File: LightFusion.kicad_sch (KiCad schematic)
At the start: 41 parts, among them IC2 ADS1292IPBSR, U1 BMD-350-A-R

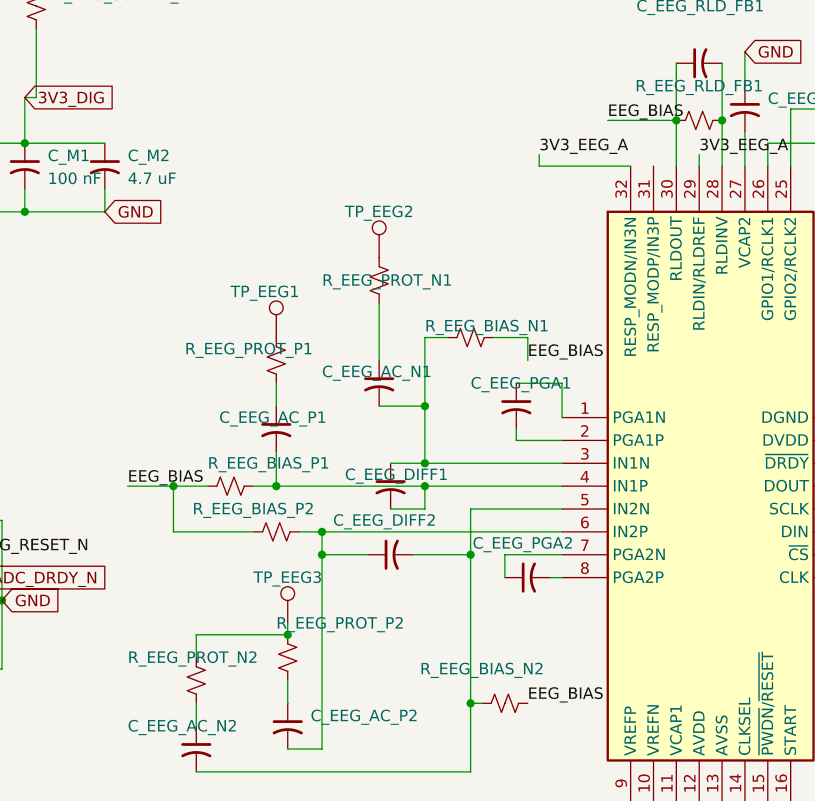
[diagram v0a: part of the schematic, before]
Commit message: remove silk screen removed from pcb
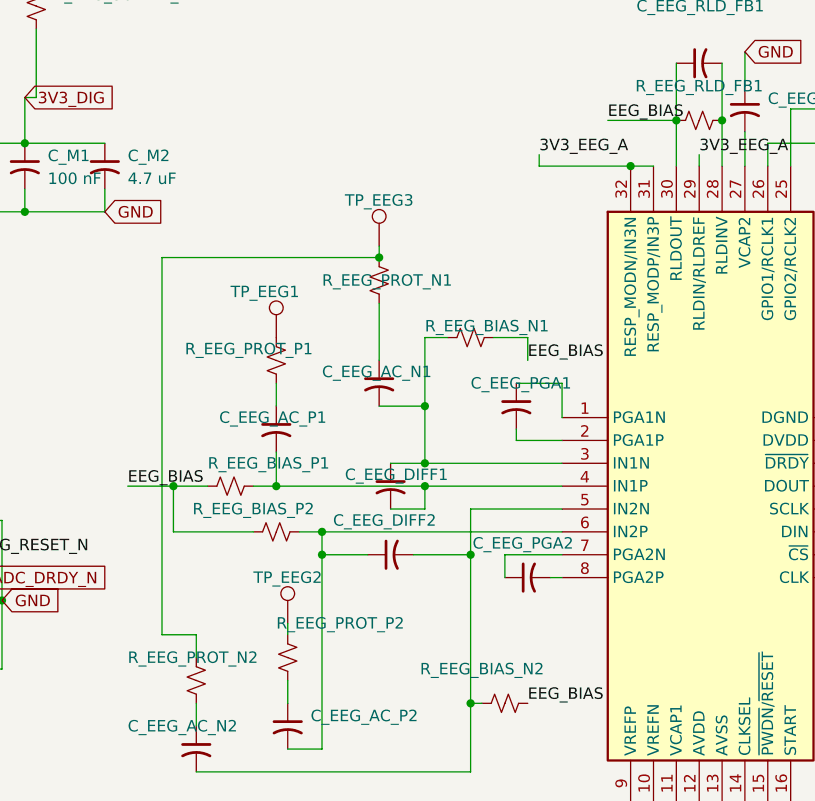
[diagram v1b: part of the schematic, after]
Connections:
- net 3V3_EEG_A: now also IC2.31 (RESP_MODP/IN3P)
- net at R_EEG_PROT_N1.1: now also R_EEG_PROT_N2.1, TP_EEG3.1; no longer TP_EEG2.1
- new net: R_EEG_PROT_P2.1, TP_EEG2.1
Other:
- moved on the sheet: TP_EEG2, TP_EEG3
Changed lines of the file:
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@@
 	)
 	(junction
+		(at 205.74 63.5)
+		(diameter 0)
+		(color 0 0 0 0)
+	)
+	(junction
 		(at 187.96 123.19)
 		(diameter 0)
@@
 	)
 	(junction
-		(at 167.64 115.57)
-		(diameter 0)
-		(color 0 0 0 0)
-	)
-	(junction
 		(at 210.82 58.42)
 		(diameter 0)
@@
 	)
 	(junction
+		(at 177.8 73.66)
+		(diameter 0)
+		(color 0 0 0 0)
+	)
+	(junction
 		(at 229.87 152.4)
 		(diameter 0)
@@
 	(wire
 		(pts
+			(xy 153.67 73.66) (xy 177.8 73.66)
+		)
+		(stroke
+			(width 0)
+			(type default)
+		)
+	)
+	(wire
+		(pts
 			(xy 171.45 106.68) (xy 176.53 106.68)
 		)
@@
 	(wire
 		(pts
+			(xy 205.74 63.5) (xy 208.28 63.5)
+		)
+		(stroke
+			(width 0)
+			(type default)
+		)
+	)
+	(wire
+		(pts
 			(xy 154.94 99.06) (xy 158.75 99.06)
 		)
@@
 	(wire
 		(pts
-			(xy 167.64 115.57) (xy 157.48 115.57)
-		)
-		(stroke
-			(width 0)
-			(type default)
-		)
-	)
-	(wire
-		(pts
 			(xy 208.28 137.16) (xy 205.74 137.16)
 		)
@@
 	(wire
 		(pts
+			(xy 153.67 115.57) (xy 153.67 73.66)
+		)
+		(stroke
+			(width 0)
+			(type default)
+		)
+	)
+	(wire
+		(pts
 			(xy 223.52 57.15) (xy 257.81 57.15)
 		)
@@
 	(wire
 		(pts
+			(xy 177.8 72.39) (xy 177.8 73.66)
+		)
+		(stroke
+			(width 0)
+			(type default)
+		)
+	)
+	(wire
+		(pts
 			(xy 251.46 144.78) (xy 251.46 147.32)
 		)
@@
 	(wire
 		(pts
+			(xy 157.48 115.57) (xy 153.67 115.57)
+		)
+		(stroke
+			(width 0)
+			(type default)
+		)
+	)
+	(wire
+		(pts
 			(xy 168.91 104.14) (xy 171.45 104.14)
 		)
@@
 	(symbol
 		(lib_id "TestPoint:TestPoint")
-		(at 177.8 73.66 0)
+		(at 167.64 114.3 0)
 		(unit 1)
 		(body_style 1)
@@
 		(dnp no)
 		(property "Reference" "TP_EEG2"
-			(at 173.99 68.58 0)
+			(at 163.83 109.22 0)
 			(show_name no)
 			(do_not_autoplace no)
@@
 		)
 		(property "Value" "TestPoint"
-			(at 180.34 71.6279 0)
+			(at 170.18 112.2679 0)
 			(hide yes)
 			(show_name no)
@@
 		)
 		(property "Footprint" "LightFusion:MILL-MAX_0906-0-15-20-76-14-11-0"
-			(at 182.88 73.66 0)
+			(at 172.72 114.3 0)
 			(hide yes)
 			(show_name no)
@@
 		)
 		(property "Datasheet" ""
-			(at 182.88 73.66 0)
+			(at 172.72 114.3 0)
 			(hide yes)
 			(show_name no)
@@
 		)
 		(property "Description" "test point"
-			(at 177.8 73.66 0)
+			(at 167.64 114.3 0)
 			(hide yes)
 			(show_name no)
@@
 	(symbol
 		(lib_id "TestPoint:TestPoint")
-		(at 167.64 114.3 0)
+		(at 177.8 72.39 0)
 		(unit 1)
 		(body_style 1)
@@
 		(dnp no)
 		(property "Reference" "TP_EEG3"
-			(at 163.83 109.22 0)
+			(at 173.99 67.31 0)
 			(show_name no)
 			(do_not_autoplace no)
@@
 		)
 		(property "Value" "TestPoint"
-			(at 170.18 112.2679 0)
+			(at 180.34 70.3579 0)
 			(hide yes)
 			(show_name no)
@@
 		)
 		(property "Footprint" "LightFusion:MILL-MAX_0906-0-15-20-76-14-11-0"
-			(at 172.72 114.3 0)
+			(at 182.88 72.39 0)
 			(hide yes)
 			(show_name no)
@@
 		)
 		(property "Datasheet" ""
-			(at 172.72 114.3 0)
+			(at 182.88 72.39 0)
 			(hide yes)
 			(show_name no)
@@
 		)
 		(property "Description" "test point"
-			(at 167.64 114.3 0)
+			(at 177.8 72.39 0)
 			(hide yes)
 			(show_name no)

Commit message: final verifications
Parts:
- added C_STIM_VCC1, C_STIM_VM1: 100 nF, LightFusion:C_0603_1608Metric, symbol C_Small_US:C_Small_US
- added C_STIM_VM2: 1 µF, LightFusion:C_0603_1608Metric, symbol C_Small_US:C_Small_US
- added R_SLEEP_PD1, R_STIM_IN1, R_STIM_IN2: 100 kΩ, LightFusion:R_0603_1608Metric, symbol R_Small_US:R_Small_US
- added R_STIM_N1, R_STIM_P1: 22 kΩ, LightFusion:R_0603_1608Metric, symbol R_Small_US:R_Small_US
- added R_STIM_PD1, R_STIM_PD2: 1 MΩ, LightFusion:R_0603_1608Metric, symbol R_Small_US:R_Small_US
- added STIM_E_N1, STIM_E_P1: (no value), LightFusion:MILL-MAX_0906-0-15-20-76-14-11-0, symbol Electrode_MillMax_0906:Electrode_MillMax_0906
- added U4: DRV8837DSGR, LightFusion:DRV8837DSGR, symbol DRV8837DSGR:DRV8837DSGR
- E_EEG1: renamed from TP_EEG1; value TestPoint -> (none); symbol TestPoint:TestPoint -> Electrode_MillMax_0906:Electrode_MillMax_0906; now not fitted
- E_EEG2: renamed from TP_EEG2; value TestPoint -> (none); symbol TestPoint:TestPoint -> Electrode_MillMax_0906:Electrode_MillMax_0906; now not fitted
- E_EEG3: renamed from TP_EEG3; value TestPoint -> (none); symbol TestPoint:TestPoint -> Electrode_MillMax_0906:Electrode_MillMax_0906; now not fitted
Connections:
- net 3V3_DIG: now also C_STIM_VCC1.1, U4.8 (VCC)
- net GND: now also C_STIM_VCC1.2, C_STIM_VM1.2, C_STIM_VM2.2, R_SLEEP_PD1.1, R_STIM_IN1.2, R_STIM_IN2.2, R_STIM_PD1.2, R_STIM_PD2.2, U4.4 (GND), U4.9 (EXP)
- net MCU_STIM_IN2: now reaches U1.21 (P0.05)
- net MCU_STIM_IN2: now also R_STIM_IN2.1, U4.5 (IN2)
- net MCU_STIM_IN1: now reaches U1.27 (P0.04)
- net MCU_STIM_IN1: now also R_STIM_IN1.1, U4.6 (IN1)
- net MCU_STIM_EN: now reaches U1.44 (P0.03)
- net MCU_STIM_EN: now also R_SLEEP_PD1.2, U4.7 (~{SLEEP})
- new net: R_STIM_N1.1, U4.3 (OUT2)
- new net: R_STIM_N1.2, R_STIM_PD2.1, STIM_E_N1.1
- new net: R_STIM_P1.1, U4.2 (OUT1)
- new net: R_STIM_P1.2, R_STIM_PD1.1, STIM_E_P1.1
- new net VBAT_SYSTEM: C_STIM_VM1.1, C_STIM_VM2.1, U4.1 (VM)
- no-connect marks 20 -> 17

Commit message: All schematic and pcb checks passed
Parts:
- U1: Arrow Part Number BMD-350-A-R -> (none); Arrow Price/Stock https://www.arrow.com/en/products/bmd-350-a-r/rigado -> (none); Manufacturer_Name Rigado -> (none); Manufacturer_Part_Number BMD-350-A-R -> (none); Mouser Part Number 377-BMD350AR -> (none); Mouser Price/Stock https://www.mouser.com/Search/Refine.aspx?Keyword=377-BMD35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 -> (none)
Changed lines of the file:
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@@
-			)
-		)
-		(property "Height" ""
-			(at 129.54 460.96 0)
-			(hide yes)
-			(show_name no)
-			(do_not_autoplace no)
-			(effects
-				(font
-					(size 1.27 1.27)
-				)
-				(justify left top)
-			)
-		)
-		(property "Manufacturer_Name" "Rigado"
-			(at 129.54 560.96 0)
-			(hide yes)
-			(show_name no)
-			(do_not_autoplace no)
-			(effects
-				(font
-					(size 1.27 1.27)
-				)
-				(justify left top)
-			)
-		)
-		(property "Manufacturer_Part_Number" "BMD-350-A-R"
-			(at 129.54 660.96 0)
-			(hide yes)
-			(show_name no)
-			(do_not_autoplace no)
-			(effects
-				(font
-					(size 1.27 1.27)
-				)
-				(justify left top)
-			)
-		)
-		(property "Mouser Part Number" "377-BMD350AR"
-			(at 129.54 760.96 0)
-			(hide yes)
-			(show_name no)
-			(do_not_autoplace no)
-			(effects
-				(font
-					(size 1.27 1.27)
-				)
-				(justify left top)
-			)
-		)
-		(property "Mouser Price/Stock" "https://www.mouser.com/Search/Refine.aspx?Keyword=377-BMD350AR"
-			(at 129.54 860.96 0)
-			(hide yes)
-			(show_name no)
-			(do_not_autoplace no)
-			(effects
-				(font
-					(size 1.27 1.27)
-				)
-				(justify left top)
-			)
-		)
-		(property "Arrow Part Number" "BMD-350-A-R"
-			(at 129.54 960.96 0)
-			(hide yes)
-			(show_name no)
-			(do_not_autoplace no)
-			(effects
-				(font
-					(size 1.27 1.27)
-				)
-				(justify left top)
-			)
-		)
-		(property "Arrow Price/Stock" "https://www.arrow.com/en/products/bmd-350-a-r/rigado"
-			(at 129.54 1060.96 0)
-			(hide yes)
-			(show_name no)
-			(do_not_autoplace no)
-			(effects
-				(font
-					(size 1.27 1.27)
-				)
-				(justify left top)
 			)
 		)

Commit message: Add new electrode positions to positions.csv
- Added D_730 and D_850 at specified coordinates on the bottom layer.
- Introduced E_EEG1, E_EEG2, and E_EEG3 at new coordinates on the bottom layer.
- Included STIM_E_N1 and STIM_E_P1 at new coordinates on the bottom layer.
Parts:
- E_EEG1, E_EEG2, E_EEG3, STIM_E_N1, STIM_E_P1: now fitted
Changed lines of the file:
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@@
 		(on_board yes)
 		(in_pos_files yes)
-		(dnp yes)
+		(dnp no)
 		(property "Reference" "E_EEG1"
 			(at 161.29 77.47 0)
@@
 		(on_board yes)
 		(in_pos_files yes)
-		(dnp yes)
+		(dnp no)
 		(property "Reference" "STIM_E_N1"
 			(at 142.24 154.94 0)
@@
 		(in_bom yes)
 		(on_board yes)
-		(in_pos_files no)
-		(dnp yes)
+		(in_pos_files yes)
+		(dnp no)
 		(property "Reference" "E_EEG2"
 			(at 163.83 109.22 0)
@@
 		(in_bom yes)
 		(on_board yes)
-		(in_pos_files no)
-		(dnp yes)
+		(in_pos_files yes)
+		(dnp no)
 		(property "Reference" "STIM_E_P1"
 			(at 137.16 148.59 0)
@@
 		(in_bom yes)
 		(on_board yes)
-		(in_pos_files no)
-		(dnp yes)
+		(in_pos_files yes)
+		(dnp no)
 		(property "Reference" "E_EEG3"
 			(at 173.99 67.31 0)

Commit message: changed EEG input filter capacitors from 0603 to 1206 because of availability issue on JLC
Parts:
- C_EEG_AC_N1, C_EEG_AC_N2, C_EEG_AC_P1, C_EEG_AC_P2: footprint LightFusion:C_0603_1608Metric -> LightFusion:C_1206_3216Metric
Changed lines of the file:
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@@
 			)
 		)
-		(property "Footprint" "LightFusion:C_0603_1608Metric"
+		(property "Footprint" "LightFusion:C_1206_3216Metric"
 			(at 167.64 125.73 0)
 			(hide yes)
@@
 			)
 		)
-		(property "Footprint" "LightFusion:C_0603_1608Metric"
+		(property "Footprint" "LightFusion:C_1206_3216Metric"
 			(at 157.48 128.27 0)
 			(hide yes)
@@
 			)
 		)
-		(property "Footprint" "LightFusion:C_0603_1608Metric"
+		(property "Footprint" "LightFusion:C_1206_3216Metric"
 			(at 166.37 92.71 0)
 			(hide yes)
@@
 			)
 		)
-		(property "Footprint" "LightFusion:C_0603_1608Metric"
+		(property "Footprint" "LightFusion:C_1206_3216Metric"
 			(at 177.8 87.63 0)
 			(hide yes)

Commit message: sync with available parts on JLC
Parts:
- C_EEG_AVDD_10U1, C_EEG_DVDD_10U1, C_EEG_REF_10U1: footprint LightFusion:C_0805_2012Metric -> LightFusion:C_0603_1608Metric
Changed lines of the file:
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@@
 			)
 		)
-		(property "Footprint" "LightFusion:C_0805_2012Metric"
+		(property "Footprint" "LightFusion:C_0603_1608Metric"
 			(at 251.46 149.86 0)
 			(hide yes)
@@
 			)
 		)
-		(property "Footprint" "LightFusion:C_0805_2012Metric"
+		(property "Footprint" "LightFusion:C_0603_1608Metric"
 			(at 262.89 101.6 0)
 			(hide yes)
@@
 			)
 		)
-		(property "Footprint" "LightFusion:C_0805_2012Metric"
+		(property "Footprint" "LightFusion:C_0603_1608Metric"
 			(at 208.28 143.51 0)
 			(hide yes)

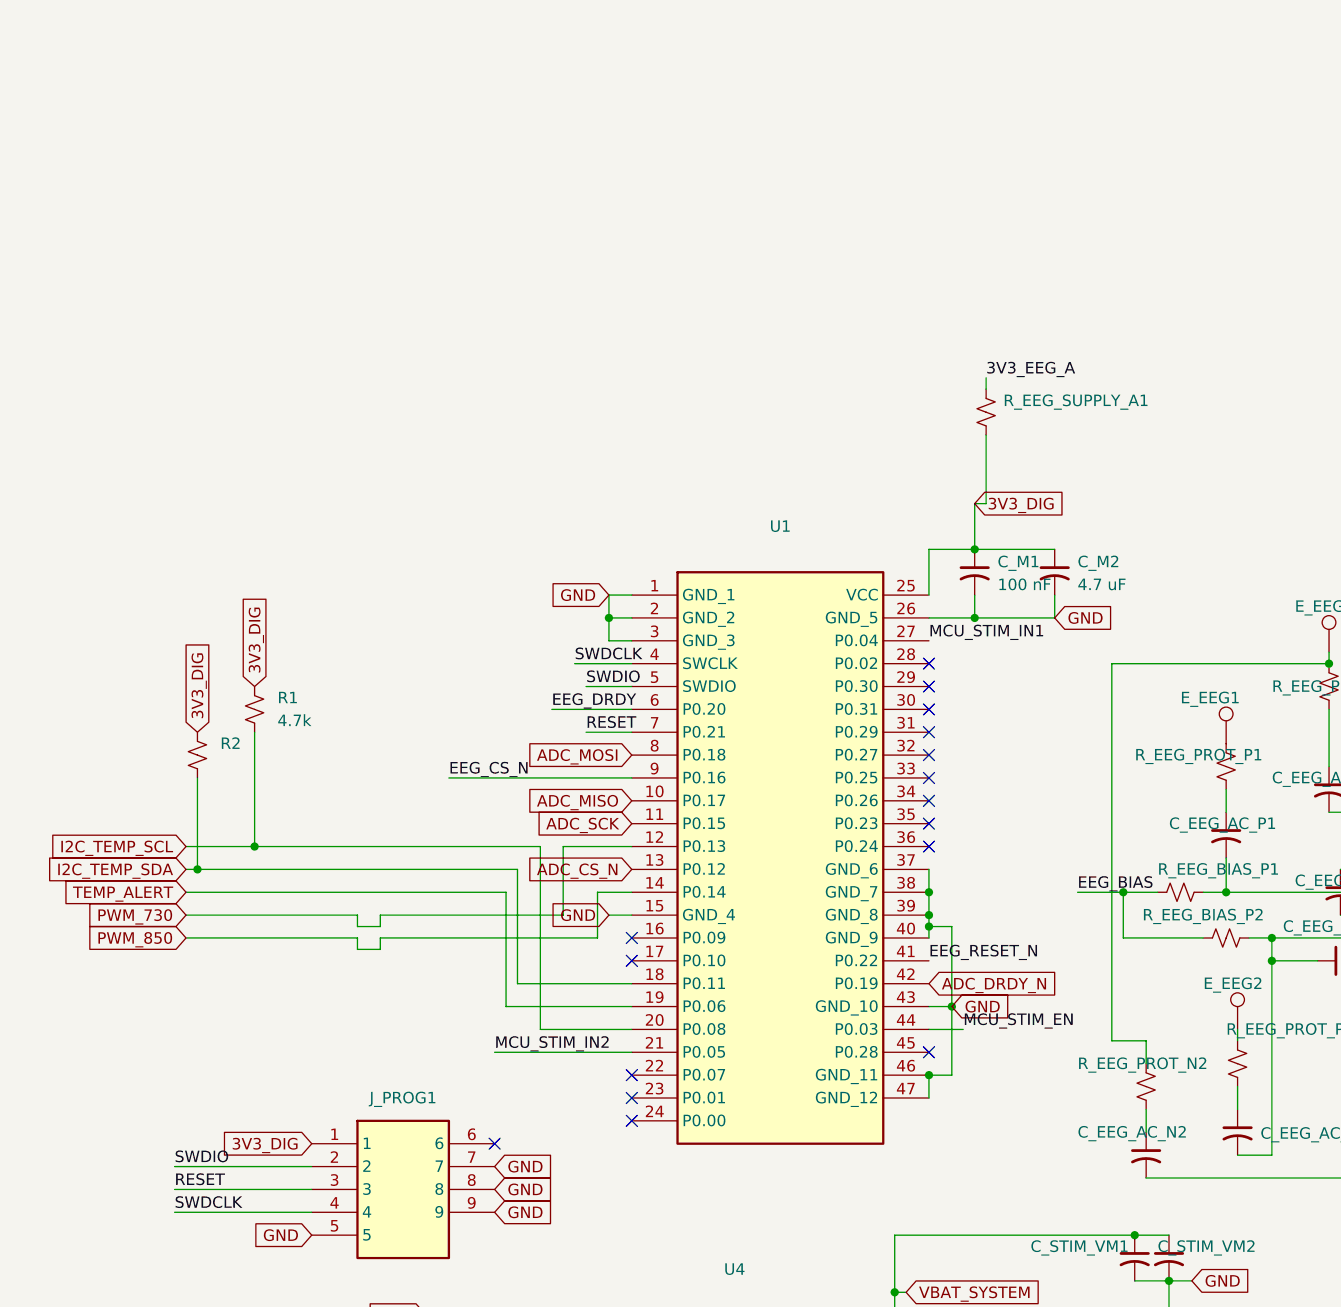
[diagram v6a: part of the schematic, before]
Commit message: redesigned MCU part to be able to solder with iron
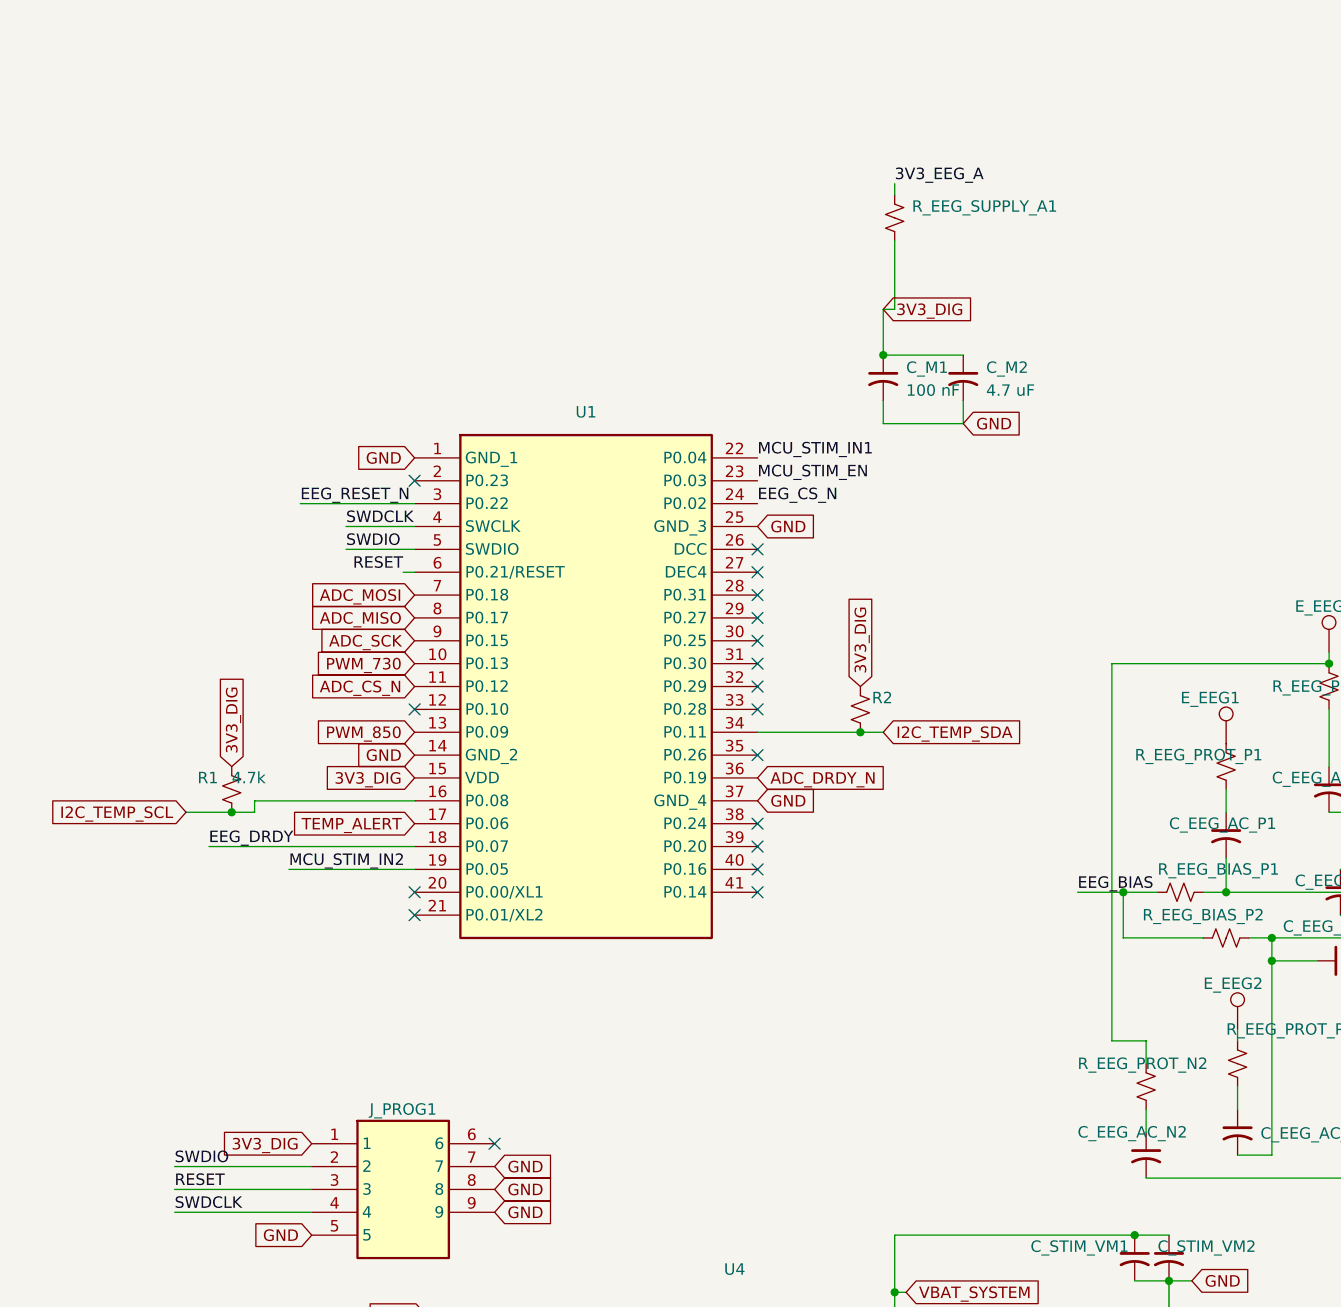
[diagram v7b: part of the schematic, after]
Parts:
- U1: value BMD-350-A-R -> MDBT42-512KV2; footprint LightFusion:BMD-350 -> LightFusion:MDBT42512KV2; symbol BMD-350-A-R:BMD-350-A-R -> MDBT42-512KV2:MDBT42-512KV2; Availability (none) -> In Stock; Check_prices (none) -> https://www.snapeda.com/parts/MDBT42Q-512KV2/Raytac+Corpora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; Height (none) -> 2; MANUFACTURER (none) -> Raytac; MAXIMUM_PACKAGE_HEIGHT (none) -> 2.2mm; MF (none) -> Raytac Corporation; MP (none) -> MDBT42Q-512KV2; Manufacturer_Name (none) -> Raytac; Manufacturer_Part_Number (none) -> MDBT42-512KV2; PARTREV (none) -> J; Package (none) -> SMD-41 Raytac Corporation; Price (none) -> None; STANDARD (none) -> Manufacturer Recommendations; SnapEDA_Link (none) -> https://www.snapeda.com/parts/MDBT42Q-512KV2/Raytac+Corpora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
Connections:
- net 3V3_DIG: now also U1.15 (VDD); no longer U1.25 (VCC)
- net ADC_CS_N: now also U1.11 (P0.12); no longer U1.13 (P0.12)
- net ADC_DRDY_N: now also U1.36 (P0.19); no longer U1.42 (P0.19)
- net ADC_MISO: now also U1.8 (P0.17); no longer U1.10 (P0.17)
- net ADC_MOSI: now also U1.7 (P0.18); no longer U1.8 (P0.18)
- net ADC_SCK: now also U1.9 (P0.15); no longer U1.11 (P0.15)
- net EEG_CS_N: now also U1.24 (P0.02); no longer U1.9 (P0.16)
- net EEG_DRDY: now also U1.18 (P0.07); no longer U1.6 (P0.20)
- net EEG_RESET_N: now also U1.3 (P0.22); no longer U1.41 (P0.22)
- net GND: now also U1.14 (GND_2), U1.25 (GND_3); no longer U1.15 (GND_4), U1.2 (GND_2), U1.26 (GND_5), U1.3 (GND_3), U1.38 (GND_7), U1.39 (GND_8), U1.40 (GND_9), U1.43 (GND_10), U1.46 (GND_11), U1.47 (GND_12)
- net I2C_TEMP_SCL: now also U1.16 (P0.08); no longer U1.20 (P0.08)
- net I2C_TEMP_SDA: now also U1.34 (P0.11); no longer U1.18 (P0.11)
- net MCU_STIM_EN: now also U1.23 (P0.03); no longer U1.44 (P0.03)
- net MCU_STIM_IN1: now also U1.22 (P0.04); no longer U1.27 (P0.04)
- net MCU_STIM_IN2: now also U1.19 (P0.05); no longer U1.21 (P0.05)
- net PWM_730: now also U1.10 (P0.13); no longer U1.12 (P0.13)
- net PWM_850: now also U1.13 (P0.09); no longer U1.14 (P0.14)
- net RESET: now also U1.6 (P0.21/RESET); no longer U1.7 (P0.21)
- net TEMP_ALERT: now also U1.17 (P0.06); no longer U1.19 (P0.06)
- no-connect marks 17 -> 19
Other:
- moved on the sheet: C_M1, C_M2, R1, R2, R_EEG_SUPPLY_A1

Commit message: final version with bom and placement
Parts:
- renumbered C_EEG_AC_N1 to C1, C_EEG_DVDD_100N1 to C10, C_EEG_PGA1 to C11, C_EEG_PGA2 to C12, C_EEG_REF_10U1 to C13, C_EEG_REF_100N1 to C14, C_EEG_RLD_FB1 to C15, C_EEG_VCAP1 to C16, C_EEG_VCAP2 to C17, C_M1 to C18, C_M2 to C19, C_EEG_AC_N2 to C2, C_STIM_VCC1 to C20, C_STIM_VM1 to C21, C_STIM_VM2 to C22, C_EEG_AC_P1 to C3, C_EEG_AC_P2 to C4, C_EEG_AVDD_10U1 to C5, C_EEG_AVDD_100N1 to C6, C_EEG_DIFF1 to C7, C_EEG_DIFF2 to C8, C_EEG_DVDD_10U1 to C9, E_EEG1 to E1, E_EEG2 to E2, E_EEG3 to E3, STIM_E_N1 to E4, STIM_E_P1 to E5, J_PROG1 to J2, R_EEG_PROT_N1 to R10, R_EEG_PROT_N2 to R11, R_EEG_PROT_P1 to R12, R_EEG_PROT_P2 to R13, R_EEG_RESET_PD1 to R14, R_EEG_RLD_FB1 to R15, R_EEG_SUPPLY_A1 to R16, R_SLEEP_PD1 to R17, R_STIM_IN1 to R18, R_STIM_IN2 to R19, R_STIM_N1 to R20, R_STIM_P1 to R21, R_STIM_PD1 to R22, R_STIM_PD2 to R23, R_EEG_BIAS_N1 to R3, R_EEG_BIAS_N2 to R4, R_EEG_BIAS_P1 to R5, R_EEG_BIAS_P2 to R6, R_EEG_CS_PU1 to R7, R_EEG_GPIO1 to R8, R_EEG_GPIO2 to R9, IC2 to U5
